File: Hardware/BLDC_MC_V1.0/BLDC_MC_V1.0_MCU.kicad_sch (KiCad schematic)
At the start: 31 parts, among them J3 USB_C_Receptacle_USB2.0_16P, J4 Conn_02x03_Counter_Clockwise, SW1 SW_Push, U4 STM32G431RBTx, U9 USBLC6-2SC6, Y1 7M-24.000MAAJ-T, Y2 ABS07-32.768KHZ-T

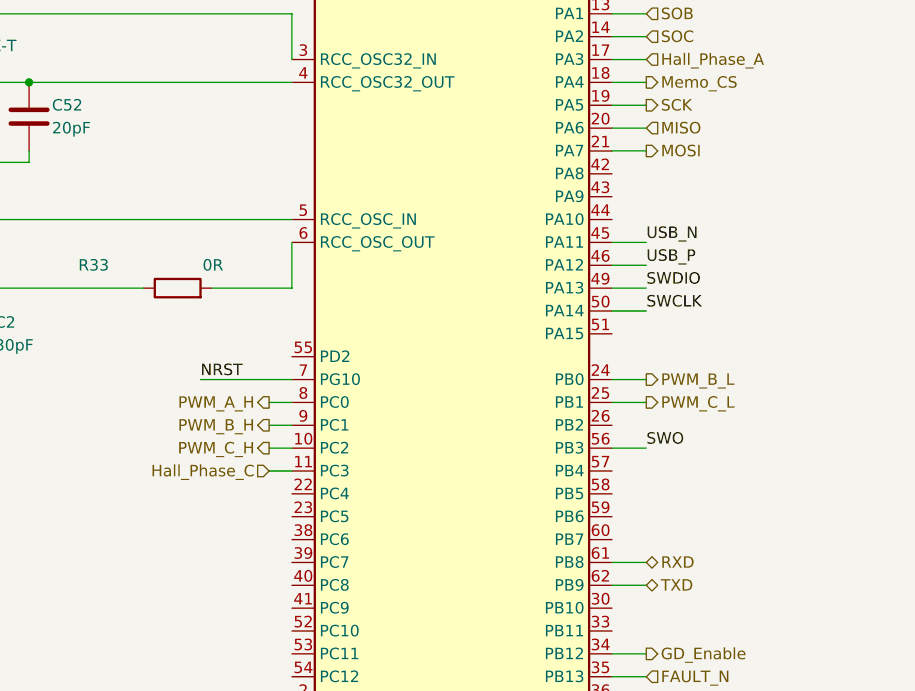
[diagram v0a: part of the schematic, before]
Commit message: Add voltage sensor to measure the 3 phase voltage of inverter bridge
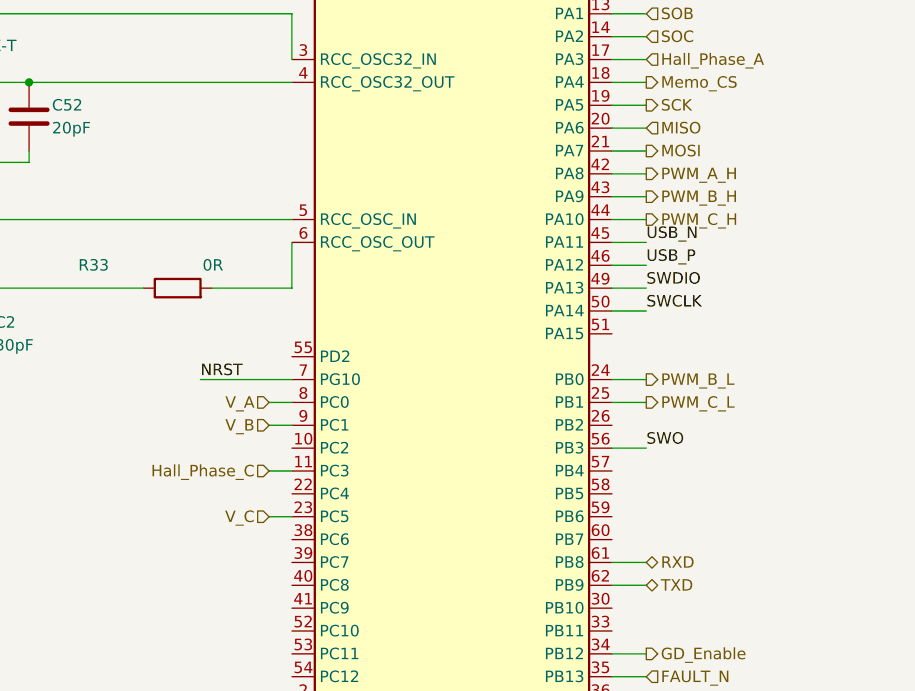
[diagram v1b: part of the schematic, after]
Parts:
- U4: Assembled (none) -> Yes; LCSC_PN (none) -> C431633; MP (none) -> STM32G431RBT6
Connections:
- net PWM_A_H: now also U4.42 (PA8); no longer U4.8 (PC0)
- net PWM_B_H: now also U4.43 (PA9); no longer U4.9 (PC1)
- net PWM_C_H: now also U4.44 (PA10); no longer U4.10 (PC2)
- net V_C: now reaches U4.23 (PC5)
- new net V_A: U4.8 (PC0)
- new net V_B: U4.9 (PC1)
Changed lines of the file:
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@@
-	(wire
-		(pts
-			(xy 129.54 100.33) (xy 132.08 100.33)
-		)
-		(stroke
-			(width 0)
-			(type default)
-		)
-	)
 	(wire
 		(pts
@@
 	(wire
 		(pts
+			(xy 129.54 95.25) (xy 132.08 95.25)
+		)
+		(stroke
+			(width 0)
+			(type default)
+		)
+	)
+	(wire
+		(pts
 			(xy 144.78 41.91) (xy 144.78 31.75)
 		)
@@
 	(wire
 		(pts
+			(xy 129.54 107.95) (xy 132.08 107.95)
+		)
+		(stroke
+			(width 0)
+			(type default)
+		)
+	)
+	(wire
+		(pts
 			(xy 167.64 54.61) (xy 171.45 54.61)
 		)
@@
 	(wire
 		(pts
-			(xy 129.54 95.25) (xy 132.08 95.25)
-		)
-		(stroke
-			(width 0)
-			(type default)
-		)
-	)
-	(wire
-		(pts
 			(xy 269.24 76.2) (xy 275.59 76.2)
 		)
@@
 	(wire
 		(pts
+			(xy 167.64 69.85) (xy 171.45 69.85)
+		)
+		(stroke
+			(width 0)
+			(type default)
+		)
+	)
+	(wire
+		(pts
 			(xy 129.54 102.87) (xy 132.08 102.87)
 		)
@@
 	(wire
 		(pts
+			(xy 129.54 97.79) (xy 132.08 97.79)
+		)
+		(stroke
+			(width 0)
+			(type default)
+		)
+	)
+	(wire
+		(pts
 			(xy 78.74 59.69) (xy 78.74 52.07)
 		)
@@
 	(wire
 		(pts
-			(xy 129.54 97.79) (xy 132.08 97.79)
+			(xy 167.64 72.39) (xy 171.45 72.39)
 		)
 		(stroke
@@
 		(pts
 			(xy 78.74 59.69) (xy 86.36 59.69)
+		)
+		(stroke
+			(width 0)
+			(type default)
+		)
+	)
+	(wire
+		(pts
+			(xy 167.64 74.93) (xy 171.45 74.93)
 		)
 		(stroke
@@
 	(hierarchical_label "PWM_B_H"
 		(shape output)
-		(at 129.54 97.79 180)
-		(effects
-			(font
-				(size 1.27 1.27)
-			)
-			(justify right)
+		(at 171.45 72.39 0)
+		(effects
+			(font
+				(size 1.27 1.27)
+			)
+			(justify left)
 		)
 	)
@@
 		)
 	)
+	(hierarchical_label "V_A"
+		(shape input)
+		(at 129.54 95.25 180)
+		(effects
+			(font
+				(size 1.27 1.27)
+			)
+			(justify right)
+		)
+	)
 	(hierarchical_label "PWM_A_L"
 		(shape output)
@@
 		)
 	)
+	(hierarchical_label "V_B"
+		(shape input)
+		(at 129.54 97.79 180)
+		(effects
+			(font
+				(size 1.27 1.27)
+			)
+			(justify right)
+		)
+	)
 	(hierarchical_label "TXD"
 		(shape bidirectional)
@@
 		)
 	)
+	(hierarchical_label "V_C"
+		(shape input)
+		(at 129.54 107.95 180)
+		(effects
+			(font
+				(size 1.27 1.27)
+			)
+			(justify right)
+		)
+	)
 	(hierarchical_label "MOSI"
 		(shape output)
@@
 	(hierarchical_label "PWM_A_H"
 		(shape output)
-		(at 129.54 95.25 180)
-		(effects
-			(font
-				(size 1.27 1.27)
-			)
-			(justify right)
+		(at 171.45 69.85 0)
+		(effects
+			(font
+				(size 1.27 1.27)
+			)
+			(justify left)
 		)
 	)
@@
 	(hierarchical_label "PWM_C_H"
 		(shape output)
-		(at 129.54 100.33 180)
-		(effects
-			(font
-				(size 1.27 1.27)
-			)
-			(justify right)
+		(at 171.45 74.93 0)
+		(effects
+			(font
+				(size 1.27 1.27)
+			)
+			(justify left)
 		)
 	)
@@
 			)
 		)
-		(property "Assembled" ""
+		(property "Assembled" "Yes"
 			(at 149.86 90.17 0)
 			(effects
@@
 			)
 		)
-		(property "LCSC_PN" ""
+		(property "LCSC_PN" "C431633"
 			(at 149.86 90.17 0)
 			(effects
@@
 			)
 		)
-		(property "MP" ""
+		(property "MP" "STM32G431RBT6"
 			(at 149.86 90.17 0)
 			(effects

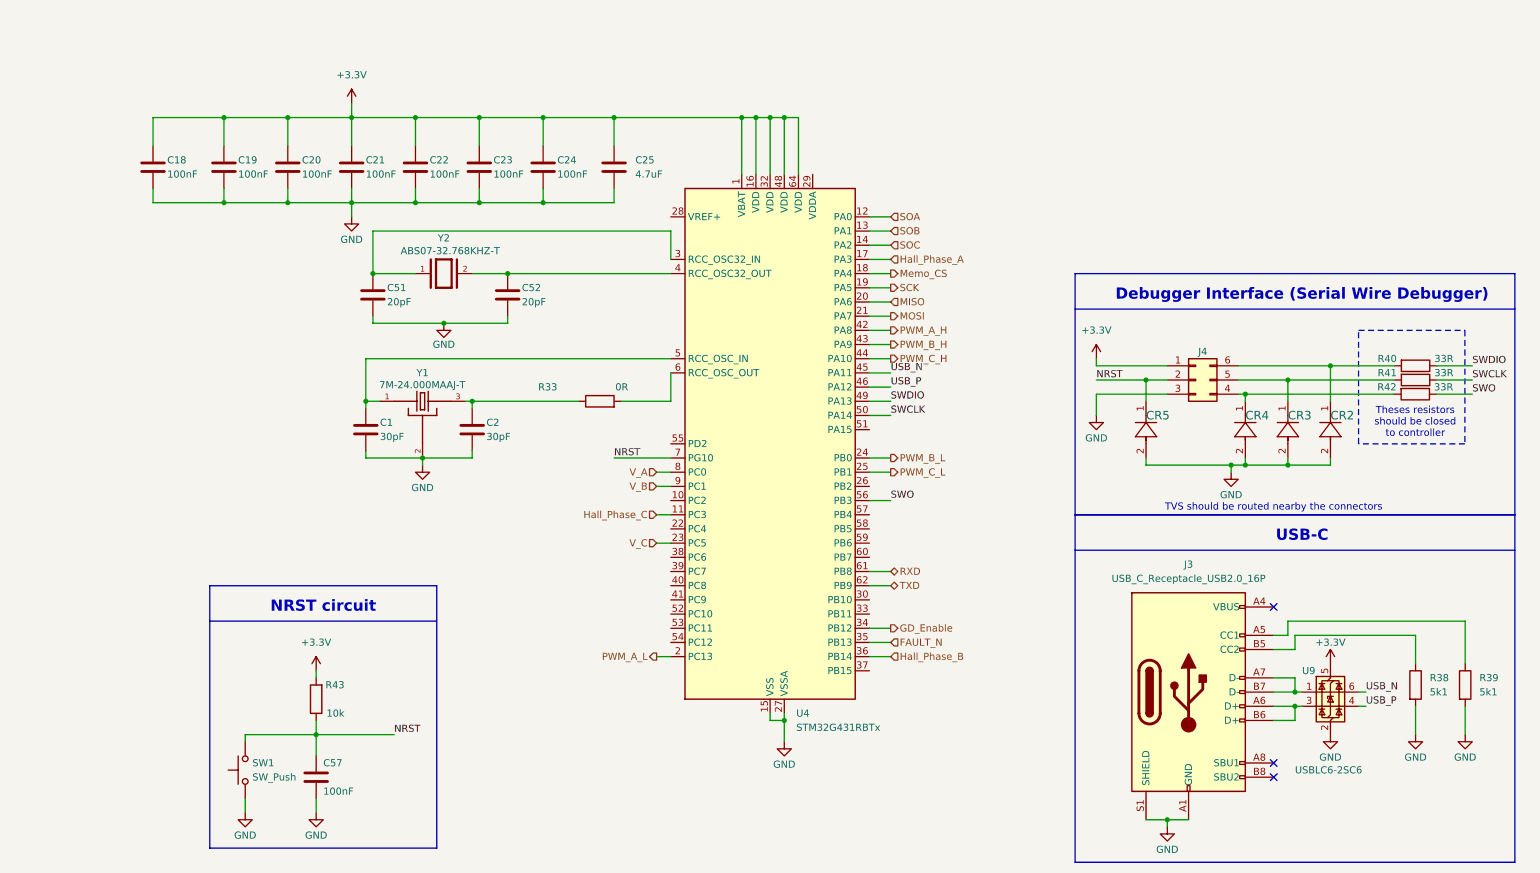
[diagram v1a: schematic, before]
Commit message: Edit the controller sheet and CAN sheet to adjust the interface between them
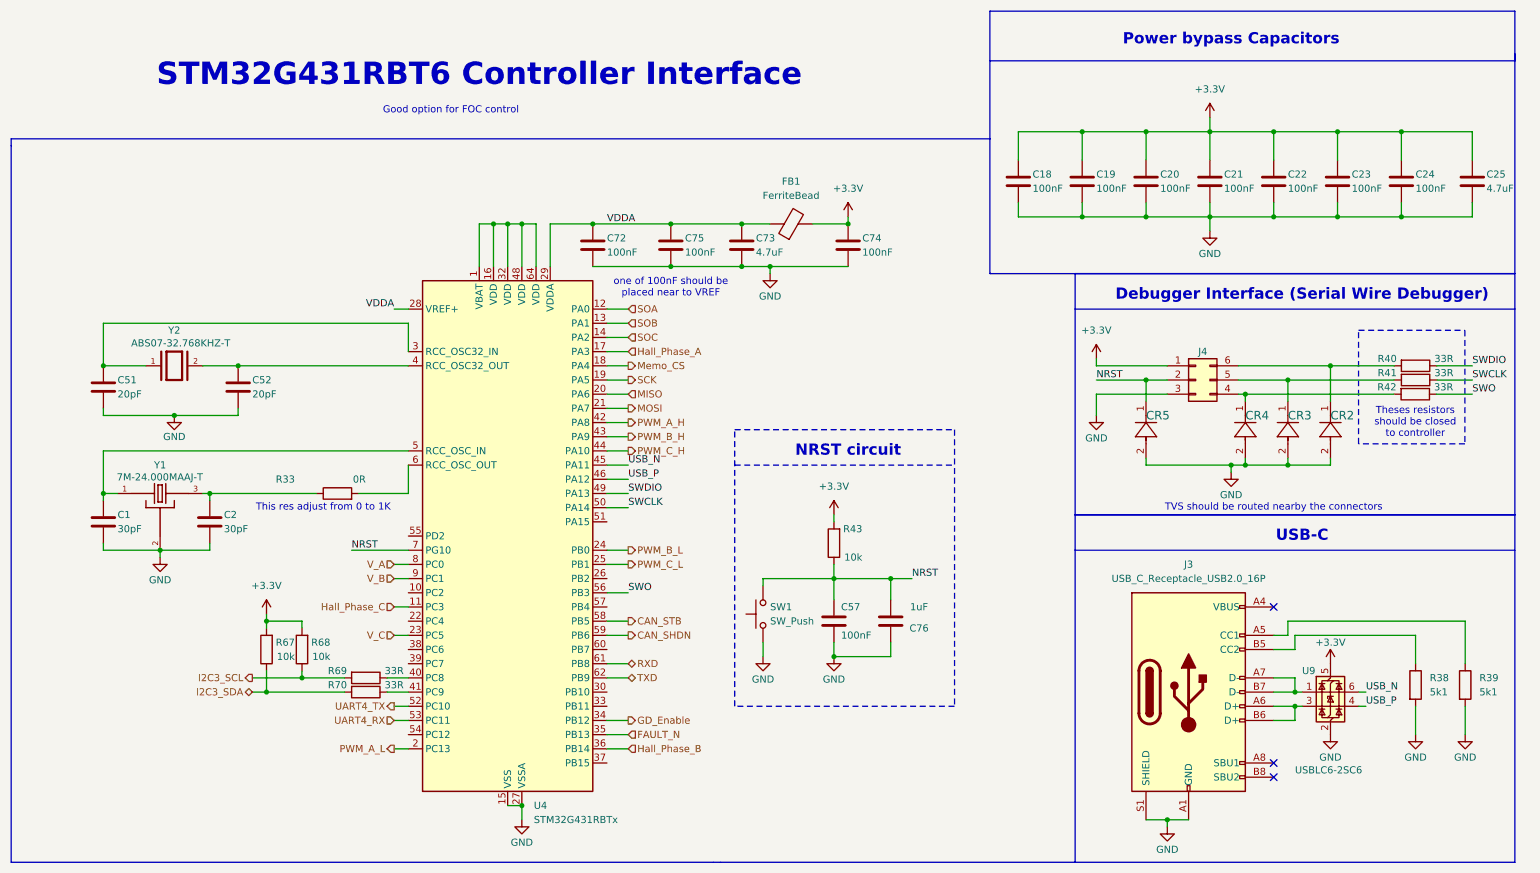
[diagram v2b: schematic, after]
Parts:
- added C72, C74, C75: 100nF, Capacitor_SMD:C_0805_2012Metric, symbol Device:C
- added C73: 4.7uF, Capacitor_SMD:C_1206_3216Metric, symbol Device:C
- added C76: 1uF, Capacitor_SMD:C_0603_1608Metric, symbol Device:C
- added FB1: FerriteBead, Inductor_SMD:L_0603_1608Metric, symbol Device:FerriteBead
- added R67, R68: 10k, Resistor_SMD:R_0603_1608Metric, symbol Device:R
- added R69, R70: 33R, Resistor_SMD:R_0603_1608Metric, symbol Device:R
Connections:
- net +3.3V: now also C74.1, FB1.2, R67.2, R68.2; no longer U4.1 (VBAT), U4.16 (VDD), U4.32 (VDD), U4.48 (VDD), U4.64 (VDD)
- net GND: now also C72.2, C73.2, C74.2, C75.2, C76.1
- net NRST: now also C76.2
- net VDDA: now reaches U4.28 (VREF+)
- net VDDA: now also U4.29 (VDDA), C72.1, C73.1, C75.1, FB1.1
- net at U4.40 (PC8): now also R69.1
- net at U4.41 (PC9): now also R70.1
- net UART4_TX: now reaches U4.52 (PC10)
- net UART4_RX: now reaches U4.53 (PC11)
- net CAN_STB: now reaches U4.58 (PB5)
- net CAN_SHDN: now reaches U4.59 (PB6)
- new net: U4.1 (VBAT), U4.16 (VDD), U4.32 (VDD), U4.48 (VDD), U4.64 (VDD)
- new net I2C3_SCL: R68.1, R69.2
- new net I2C3_SDA: R67.1, R70.2
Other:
- note added: "Good option for FOC control"
- note added: "Power bypass Capacitors"
- note added: "STM32G431RBT6 Controller Interface"
- note added: "This res adjust from 0 to 1K"
- note added: "one of 100nF should be placed near to VREF"
- moved on the sheet: C1, C18, C19, C2, C20, C21, C22, C23, C24, C25, C51, C52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

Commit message: Adjust the connections between sheets
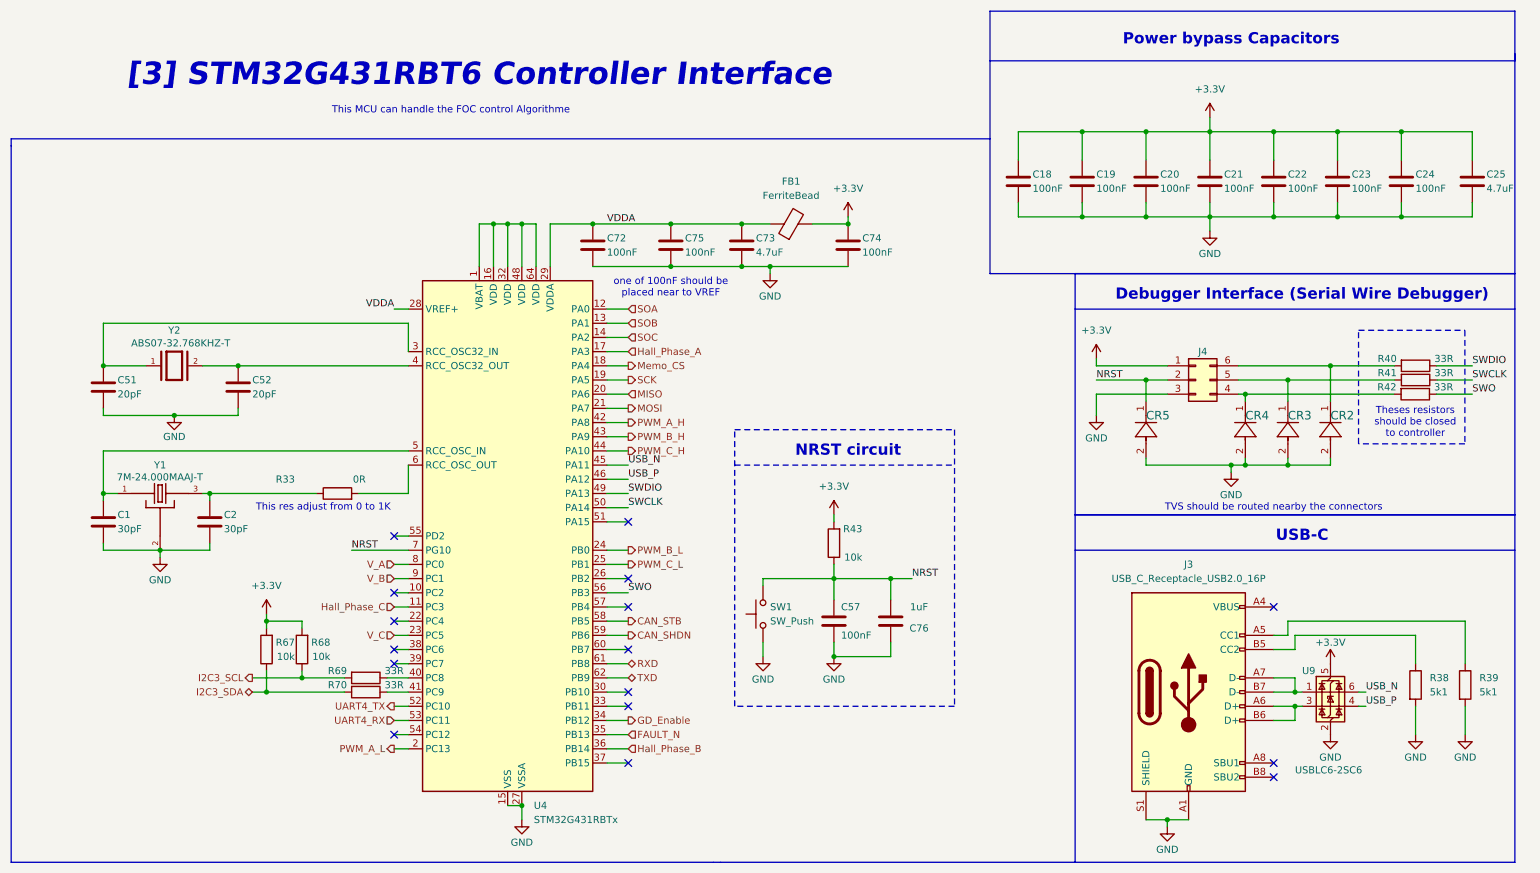
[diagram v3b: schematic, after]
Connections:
- no-connect marks 3 -> 16
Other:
- note added: "This MCU can handle the FOC control Algorithme"
- note added: "[3] STM32G431RBT6 Controller Interface"
- note removed: "Good option for FOC control"
- note removed: "STM32G431RBT6 Controller Interface"
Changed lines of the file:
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@@
 		)
 	)
-	(text "STM32G431RBT6 Controller Interface \n"
+	(text "[3] STM32G431RBT6 Controller Interface \n"
 		(exclude_from_sim no)
 		(at 97.79 24.13 0)
@@
 				(thickness 0.8)
 				(bold yes)
+				(italic yes)
 				(color 132 0 0 1)
 			)
@@
 		)
 	)
-	(text "Good option for FOC control\n"
+	(text "This MCU can handle the FOC control Algorithme"
 		(exclude_from_sim no)
 		(at 92.71 30.48 0)
@@
 	)
 	(no_connect
+		(at 124.46 104.14)
+	)
+	(no_connect
+		(at 82.55 129.54)
+	)
+	(no_connect
+		(at 124.46 147.32)
+	)
+	(no_connect
+		(at 124.46 119.38)
+	)
+	(no_connect
 		(at 240.03 147.32)
+	)
+	(no_connect
+		(at 82.55 142.24)
+	)
+	(no_connect
+		(at 124.46 134.62)
+	)
+	(no_connect
+		(at 124.46 127)
+	)
+	(no_connect
+		(at 82.55 116.84)
+	)
+	(no_connect
+		(at 82.55 127)
 	)
 	(no_connect
@@
 	)
 	(no_connect
+		(at 124.46 137.16)
+	)
+	(no_connect
+		(at 124.46 114.3)
+	)
+	(no_connect
+		(at 82.55 106.68)
+	)
+	(no_connect
 		(at 240.03 119.38)
 	)
+	(no_connect
+		(at 82.55 121.92)
+	)
 	(wire
 		(pts
@@
 	(wire
 		(pts
+			(xy 82.55 121.92) (xy 85.09 121.92)
+		)
+		(stroke
+			(width 0)
+			(type default)
+		)
+	)
+	(wire
+		(pts
 			(xy 275.59 34.29) (xy 262.89 34.29)
 		)
@@
 	(wire
 		(pts
+			(xy 124.46 134.62) (xy 120.65 134.62)
+		)
+		(stroke
+			(width 0)
+			(type default)
+		)
+	)
+	(wire
+		(pts
 			(xy 194.31 49.53) (xy 205.74 49.53)
 		)
@@
 	(wire
 		(pts
+			(xy 82.55 106.68) (xy 85.09 106.68)
+		)
+		(stroke
+			(width 0)
+			(type default)
+		)
+	)
+	(wire
+		(pts
 			(xy 66.04 121.92) (xy 66.04 123.19)
 		)
@@
 	(wire
 		(pts
+			(xy 124.46 137.16) (xy 120.65 137.16)
+		)
+		(stroke
+			(width 0)
+			(type default)
+		)
+	)
+	(wire
+		(pts
 			(xy 217.17 46.99) (xy 217.17 49.53)
 		)
@@
 	(wire
 		(pts
+			(xy 82.55 142.24) (xy 85.09 142.24)
+		)
+		(stroke
+			(width 0)
+			(type default)
+		)
+	)
+	(wire
+		(pts
+			(xy 124.46 127) (xy 120.65 127)
+		)
+		(stroke
+			(width 0)
+			(type default)
+		)
+	)
+	(wire
+		(pts
 			(xy 30.48 76.2) (xy 30.48 68.58)
 		)
@@
 	(wire
 		(pts
+			(xy 124.46 119.38) (xy 120.65 119.38)
+		)
+		(stroke
+			(width 0)
+			(type default)
+		)
+	)
+	(wire
+		(pts
 			(xy 243.84 124.46) (xy 243.84 127)
 		)
@@
 	(wire
 		(pts
+			(xy 124.46 147.32) (xy 120.65 147.32)
+		)
+		(stroke
+			(width 0)
+			(type default)
+		)
+	)
+	(wire
+		(pts
 			(xy 120.65 73.66) (xy 124.46 73.66)
 		)
@@
 	(wire
 		(pts
+			(xy 82.55 116.84) (xy 85.09 116.84)
+		)
+		(stroke
+			(width 0)
+			(type default)
+		)
+	)
+	(wire
+		(pts
 			(xy 217.17 78.74) (xy 220.98 78.74)
 		)
@@
 	(wire
 		(pts
+			(xy 124.46 104.14) (xy 120.65 104.14)
+		)
+		(stroke
+			(width 0)
+			(type default)
+		)
+	)
+	(wire
+		(pts
 			(xy 242.57 124.46) (xy 240.03 124.46)
 		)
@@
 		)
 	)
+	(wire
+		(pts
+			(xy 124.46 114.3) (xy 120.65 114.3)
+		)
+		(stroke
+			(width 0)
+			(type default)
+		)
+	)
 	(polyline
 		(pts
@@
 	(wire
 		(pts
+			(xy 82.55 129.54) (xy 85.09 129.54)
+		)
+		(stroke
+			(width 0)
+			(type default)
+		)
+	)
+	(wire
+		(pts
 			(xy 40.64 109.22) (xy 49.53 109.22)
 		)
@@
 		)
 		(stroke
+			(width 0)
+			(type default)
+		)
+	)
+	(wire
+		(pts
+			(xy 82.55 127) (xy 85.09 127)
+		)
+		(stroke
